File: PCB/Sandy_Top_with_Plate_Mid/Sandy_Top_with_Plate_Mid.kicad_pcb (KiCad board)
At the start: 2 copper layers, 285 x 75.1 mm, 70 parts, among them J1 Conn_02x02_Top_Bottom, J2 Conn_02x02_Top_Bottom, J3 Conn_02x02_Top_Bottom

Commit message: JST SH コネクタのフットプリントにコートヤードを追加
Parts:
- J1, J2, J3: footprint locallib:JST_SH_SM04B-SRSS-TB_1x04-1MP_P1.00mm_Horizontal_wCable_housing_spare_pin -> locallib:JST_SH_SM04B-SRSS-TB_1x04-1MP_P1.00mm_Horizontal_wCable_housing_spare_pin_courtyard

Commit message: シルクがハンダマスクに切り取られる箇所をフットプリントを変更して対応
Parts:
- EXT_TC0, EXT_TC1, EXT_TC2, EXT_TC3, EXT_TC4, EXT_TC5, EXT_TC6, EXT_TR0, EXT_TR1, EXT_TR2, EXT_TR5, EXT_TR6: footprint TestPoint:TestPoint_THTPad_D2.0mm_Drill1.0mm -> locallib:TestPoint_THTPad_D2.0mm_Drill1.0mm
- moved EXT_TC4 38.1 mm to (215.1, 21.0)
- moved D15 3.69 mm to (152.0, 68.7), turned to 90 degrees
- moved D10 3.57 mm to (209.2, 30.6), turned to 90 degrees
- moved D11 3.57 mm to (228.2, 30.6), turned to 90 degrees
- moved D12 3.57 mm to (247.3, 30.6), turned to 90 degrees
- moved D16 3.57 mm to (133.0, 49.6), turned to 90 degrees
- moved D17 3.57 mm to (152.0, 49.6), turned to 90 degrees
- moved D19 3.57 mm to (190.1, 49.6), turned to 90 degrees
- moved D2 3.57 mm to (56.8, 30.6), turned to 90 degrees
- moved D3 3.57 mm to (75.8, 30.6), turned to 90 degrees
- moved D6 3.57 mm to (133.0, 30.6), turned to 90 degrees
- moved D7 3.57 mm to (152.0, 30.6), turned to 90 degrees
- moved D1 3.57 mm to (37.7, 30.6), turned to 90 degrees
- moved D4 3.57 mm to (94.9, 30.6), turned to 90 degrees
- moved D5 3.57 mm to (113.9, 30.6), turned to 90 degrees
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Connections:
- J1 pad 4: Top_GND -> Top_row2
- SW_'1 pad 1: Net-(D20-A) -> Top_col4
- SW_'1 pad 2: Top_col4 -> Net-(D20-A)
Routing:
- net Top_col0: track 29.2 -> 0.00 mm

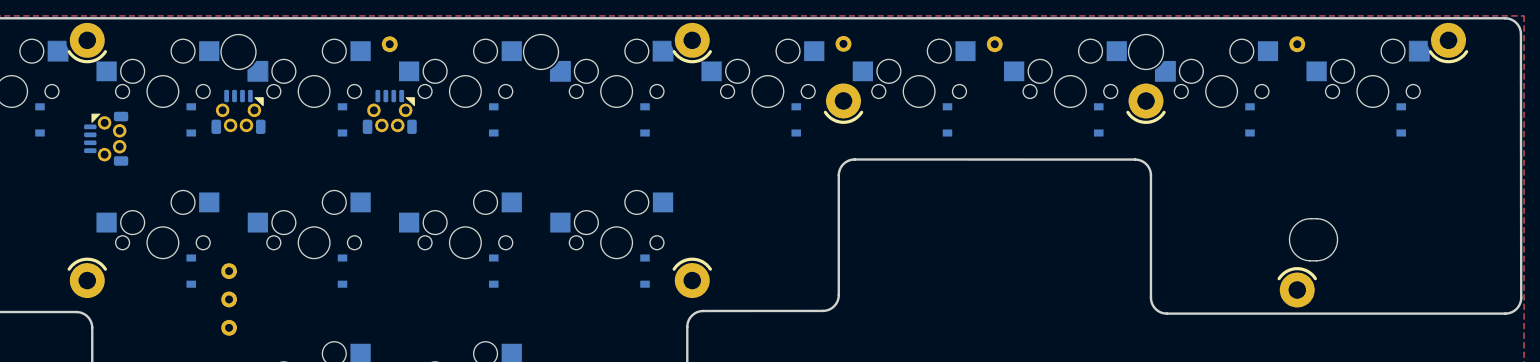
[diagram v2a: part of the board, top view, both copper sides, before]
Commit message: WIP シルクがハンダマスクに切り取られる箇所をフットプリントを変更して対応
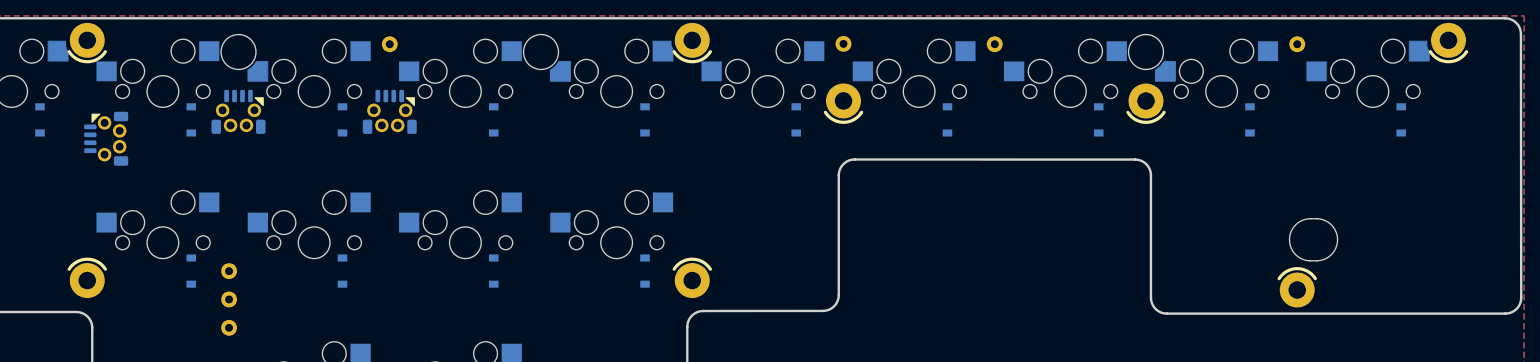
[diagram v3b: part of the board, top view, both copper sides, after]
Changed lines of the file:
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@@
 		(fp_arc
 			(start 114.175 -9.90004)
-			(mid 114.731476 -11.243582)
+			(mid 114.731482 -11.243546)
 			(end 116.075 -11.80004)
 			(stroke
@@
 		(fp_arc
 			(start 114.923491 -9.898554)
-			(mid 115.274975 -10.747086)
+			(mid 115.274981 -10.74705)
 			(end 116.123491 -11.098554)
 			(stroke
@@
 		(fp_arc
 			(start 116.075 -8.00004)
-			(mid 114.731482 -8.55651)
+			(mid 114.731447 -8.556504)
 			(end 114.175 -9.90004)
 			(stroke
@@
 		(fp_arc
 			(start 116.123491 -8.698554)
-			(mid 115.274982 -9.050056)
+			(mid 115.275017 -9.050062)
 			(end 114.923491 -9.898554)
 			(stroke
@@
 		(fp_arc
 			(start 118.923491 -11.098554)
-			(mid 119.772038 -10.747112)
+			(mid 119.772073 -10.747118)
 			(end 120.123491 -9.898554)
 			(stroke
@@
 		(fp_arc
 			(start 118.975 -11.80004)
-			(mid 120.318488 -11.243516)
+			(mid 120.318452 -11.24351)
 			(end 120.875 -9.90004)
 			(stroke
@@
 		(fp_arc
 			(start 120.123491 -9.898554)
-			(mid 119.772032 -9.050029)
+			(mid 119.772038 -9.049994)
 			(end 118.923491 -8.698554)
 			(stroke
@@
 		(fp_arc
 			(start 120.875 -9.90004)
-			(mid 120.318482 -8.556576)
+			(mid 120.318488 -8.556541)
 			(end 118.975 -8.00004)
 			(stroke
@@
 		(fp_arc
 			(start 27.975 35.345746)
-			(mid 27.389238 36.759982)
+			(mid 27.389238 36.759986)
 			(end 25.975 37.345746)
 			(stroke
@@
 		(fp_arc
 			(start 97.875 -0.60004)
-			(mid 96.460771 -1.1858)
+			(mid 96.460736 -1.185794)
 			(end 95.875 -2.60004)
 			(stroke
@@
 		(fp_arc
 			(start 140.475 -37.80004)
-			(mid 141.889198 -37.214227)
+			(mid 141.889163 -37.214221)
 			(end 142.475 -35.80004)
 			(stroke
@@
 		(fp_line
 			(start 4.572 -6.35)
-			(end 7.112 -6.35)
+			(end 6.817 -6.35)
 			(stroke
 				(width 0.15)
@@
 		)
 		(fp_line
-			(start 7.112 -6.35)
+			(start 6.817 -5.705)
+			(end 6.817 -6.35)
+			(stroke
+				(width 0.15)
+				(type solid)
+			)
+			(layer "B.CrtYd")
+		)
+		(fp_line
+			(start 7.112 -4.83)
+			(end 6.817 -5.705)
+			(stroke
+				(width 0.15)
+				(type solid)
+			)
+			(layer "B.CrtYd")
+		)
+		(fp_line
+			(start 7.112 -4.83)
 			(end 7.112 -3.81)
 			(stroke
@@
 				(gr_poly
 					(pts
-						(xy -1.25 -1.25) (xy 1 -1.25) (xy 1 -0.75) (xy 1.25 -0.2) (xy 1.25 1.25) (xy -1.25 1.25)
+						(xy -1.25 -1.25) (xy 0.95 -1.25) (xy 0.95 -0.65) (xy 1.25 0.25) (xy 1.25 1.25) (xy -1.25 1.25)
 					)
 					(width 0.12)
@@
 		(fp_line
 			(start 4.572 -6.35)
-			(end 7.112 -6.35)
+			(end 6.817 -6.35)
 			(stroke
 				(width 0.15)
@@
 		)
 		(fp_line
-			(start 7.112 -6.35)
+			(start 6.817 -5.705)
+			(end 6.817 -6.35)
+			(stroke
+				(width 0.15)
+				(type solid)
+			)
+			(layer "B.CrtYd")
+		)
+		(fp_line
+			(start 7.112 -4.83)
+			(end 6.817 -5.705)
+			(stroke
+				(width 0.15)
+				(type solid)
+			)
+			(layer "B.CrtYd")
+		)
+		(fp_line
+			(start 7.112 -4.83)
 			(end 7.112 -3.81)
 			(stroke
@@
 				(gr_poly
 					(pts
-						(xy -1.25 -1.25) (xy 1 -1.25) (xy 1 -0.75) (xy 1.25 -0.2) (xy 1.25 1.25) (xy -1.25 1.25)
+						(xy -1.25 -1.25) (xy 0.95 -1.25) (xy 0.95 -0.65) (xy 1.25 0.25) (xy 1.25 1.25) (xy -1.25 1.25)
 					)
 					(width 0.12)
@@
 		(tags "test point THT pad")
 		(property "Reference" "EXT_TR0"
-			(at -4.365625 0 360)
+			(at -4.365625 0 0)
 			(layer "B.SilkS")
 			(effects
@@
 		)
 		(property "Value" "Conn_01x01"
-			(at 0 -2.05 360)
+			(at 0 -2.05 0)
 			(layer "B.Fab")
 			(effects
@@
 		)
 		(fp_text user "${REFERENCE}"
-			(at 0 2 360)
+			(at 0 2 0)
 			(layer "B.Fab")
 			(effects

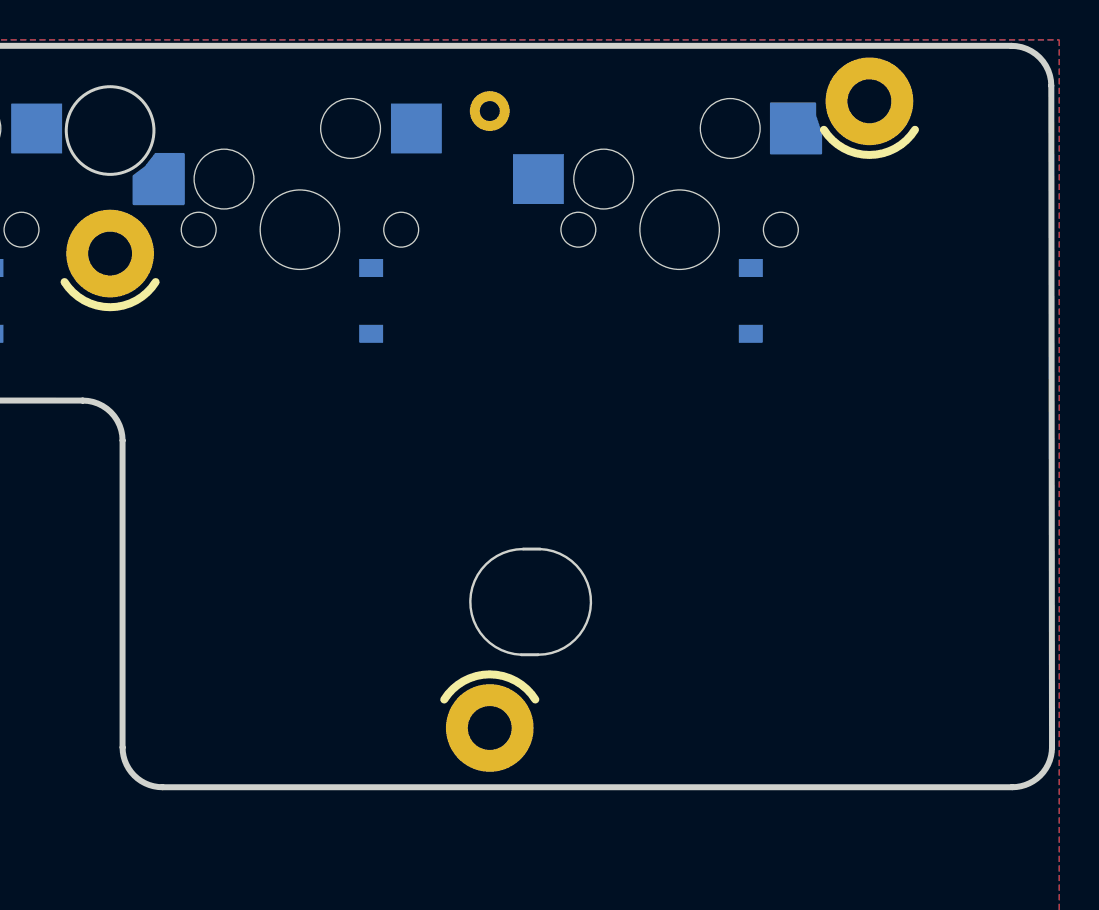
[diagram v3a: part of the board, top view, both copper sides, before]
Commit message: WIP 配線中。ハンダマスクの拡張を変更0.2→0
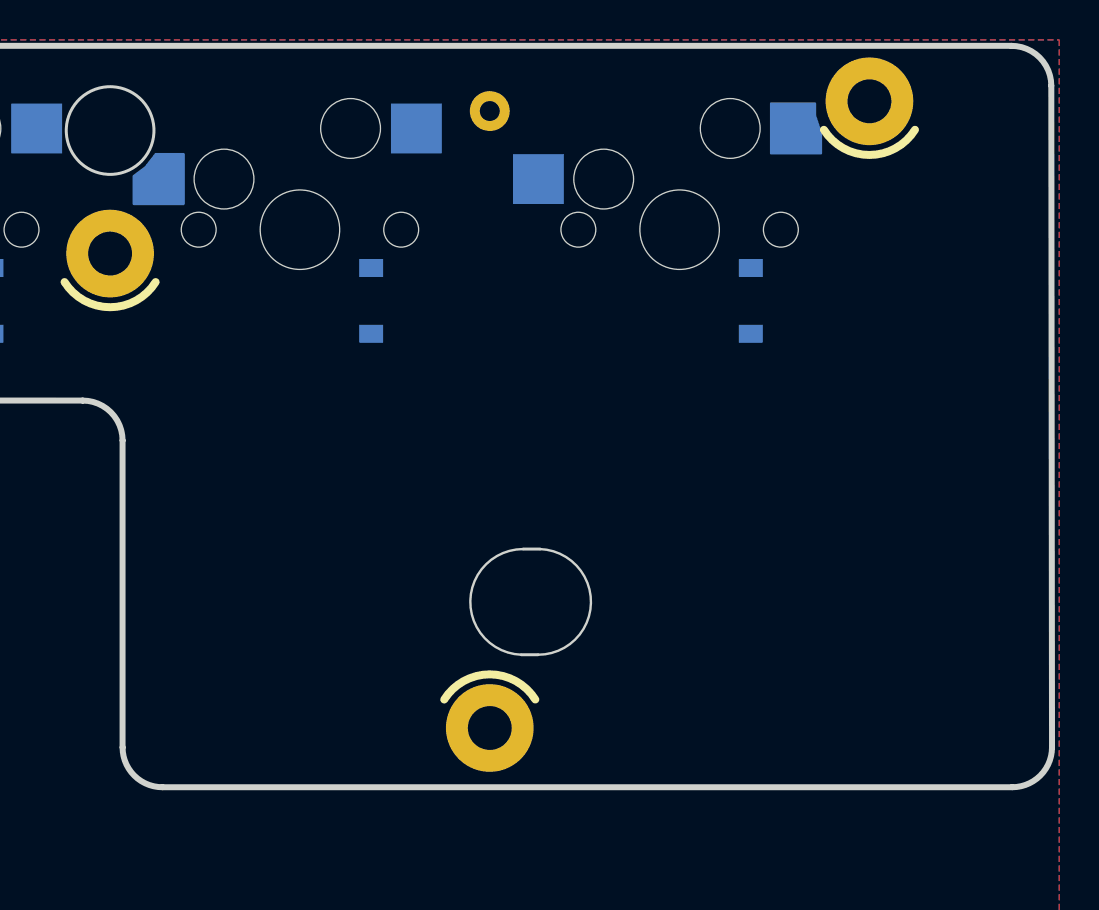
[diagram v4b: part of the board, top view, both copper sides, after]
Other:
- rule pad_to_mask_clearance: 0.2 -> 0
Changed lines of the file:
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@@
 			(dielectric_constraints no)
 		)
-		(pad_to_mask_clearance 0.2)
+		(pad_to_mask_clearance 0)
 		(allow_soldermask_bridges_in_footprints no)
 		(aux_axis_origin 15.10531 17.478405)
@@
 		(fp_arc
 			(start 114.175 -9.90004)
-			(mid 114.731482 -11.243546)
+			(mid 114.731476 -11.243582)
 			(end 116.075 -11.80004)
 			(stroke
@@
 		(fp_arc
 			(start 114.923491 -9.898554)
-			(mid 115.274981 -10.74705)
+			(mid 115.274975 -10.747086)
 			(end 116.123491 -11.098554)
 			(stroke
@@
 		(fp_arc
 			(start 116.075 -8.00004)
-			(mid 114.731447 -8.556504)
+			(mid 114.731482 -8.55651)
 			(end 114.175 -9.90004)
 			(stroke
@@
 		(fp_arc
 			(start 116.123491 -8.698554)
-			(mid 115.275017 -9.050062)
+			(mid 115.274982 -9.050056)
 			(end 114.923491 -9.898554)
 			(stroke
@@
 		(fp_arc
 			(start 118.923491 -11.098554)
-			(mid 119.772073 -10.747118)
+			(mid 119.772038 -10.747112)
 			(end 120.123491 -9.898554)
 			(stroke
@@
 		(fp_arc
 			(start 118.975 -11.80004)
-			(mid 120.318452 -11.24351)
+			(mid 120.318488 -11.243516)
 			(end 120.875 -9.90004)
 			(stroke
@@
 		(fp_arc
 			(start 120.123491 -9.898554)
-			(mid 119.772038 -9.049994)
+			(mid 119.772032 -9.050029)
 			(end 118.923491 -8.698554)
 			(stroke
@@
 		(fp_arc
 			(start 120.875 -9.90004)
-			(mid 120.318488 -8.556541)
+			(mid 120.318482 -8.556576)
 			(end 118.975 -8.00004)
 			(stroke
@@
 		(fp_arc
 			(start 27.975 35.345746)
-			(mid 27.389238 36.759986)
+			(mid 27.389238 36.759982)
 			(end 25.975 37.345746)
 			(stroke
@@
 		(fp_arc
 			(start 97.875 -0.60004)
-			(mid 96.460736 -1.185794)
+			(mid 96.460771 -1.1858)
 			(end 95.875 -2.60004)
 			(stroke
@@
 		(fp_arc
 			(start 140.475 -37.80004)
-			(mid 141.889163 -37.214221)
+			(mid 141.889198 -37.214227)
 			(end 142.475 -35.80004)
 			(stroke

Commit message: パーツ・配線微調整。Top一旦FIX（再）
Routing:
- net Top_row0: track 0.00 -> 287.5 mm, vias 0 -> 2
- net Top_row5: track 0.00 -> 279.9 mm, vias 0 -> 2
- net Top_col6: track 0.00 -> 149.6 mm, vias 0 -> 3
- net Top_col3: track 0.00 -> 136.7 mm, vias 0 -> 3
- net Top_col4: track 0.00 -> 115.3 mm, vias 0 -> 3
- net Top_col0: track 0.00 -> 109.5 mm
- net Top_row1: track 0.00 -> 96.0 mm
- net Top_col5: track 0.00 -> 92.5 mm
- net Top_row6: track 0.00 -> 92.5 mm
- net Top_row2: track 0.00 -> 85.7 mm
- net Top_col1: track 0.00 -> 77.5 mm, vias 0 -> 1
- net Top_col2: track 0.00 -> 58.3 mm, vias 0 -> 2
- net Net-(D9-A): track 0.00 -> 7.94 mm
- net Net-(D8-A): track 0.00 -> 7.94 mm
- net Net-(D7-A): track 0.00 -> 7.94 mm
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- added copper zone on B.Cu, net Top_GND
- added copper zone on F.Cu, net Top_GND
- removed copper zone on B.Cu, net Top_row0
- removed copper zone on F.Cu, net Top_row0
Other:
- board text removed: "Screw to Bottom ↓"
